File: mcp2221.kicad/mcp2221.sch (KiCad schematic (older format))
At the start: 26 parts, among them J1 Jumper 32 or 21, J2 Conn_01x04_Male, J3 Conn_01x03_Male, J4 Conn_01x06_Male, J5 Conn_01x03_Male, J6 Conn_01x06_Male, J7 Conn_01x02_Male, J8 Conn_01x02_Male, SW1 SW_Push, SW2 SW_Push, U1 AMS1117CD-3.3, U2 MCP2221

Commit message: changed to larger pads on SMD-footprints
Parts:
- C1, C2: footprint Capacitor_SMD:C_1206_3216Metric_Pad1.42x1.75mm_HandSolder -> user:C_1206_3216_Pad1.7x1.75mm_BB
- D1, D2: footprint LED_SMD:LED_1206_3216Metric_Pad1.42x1.75mm_HandSolder -> user:LED_1206_3216_Pad1.7x1.75mm_BB
- R1, R2, R3, R4, R5, R6, R7, R8, R9: footprint Resistor_SMD:R_1206_3216Metric_Pad1.42x1.75mm_HandSolder -> user:R_1206_3216_Pad1.7x1.75mm_BB
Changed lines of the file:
@@
 F 0 "R1" H 4270 3196 50  0000 L CNN
 F 1 "2.2k" H 4270 3105 50  0000 L CNN
-F 2 "Resistor_SMD:R_1206_3216Metric_Pad1.42x1.75mm_HandSolder" V 4130 3150 50  0001 C CNN
+F 2 "user:R_1206_3216_Pad1.7x1.75mm_BB" V 4130 3150 50  0001 C CNN
 F 3 "~" H 4200 3150 50  0001 C CNN
 	1    4200 3150
@@
 F 0 "R2" H 4520 3196 50  0000 L CNN
 F 1 "2.2K" H 4520 3105 50  0000 L CNN
-F 2 "Resistor_SMD:R_1206_3216Metric_Pad1.42x1.75mm_HandSolder" V 4380 3150 50  0001 C CNN
+F 2 "user:R_1206_3216_Pad1.7x1.75mm_BB" V 4380 3150 50  0001 C CNN
 F 3 "~" H 4450 3150 50  0001 C CNN
 	1    4450 3150
@@
 F 0 "R5" H 6450 4100 50  0000 L CNN
 F 1 "1K" H 6450 4000 50  0000 L CNN
-F 2 "Resistor_SMD:R_1206_3216Metric_Pad1.42x1.75mm_HandSolder" V 6580 4050 50  0001 C CNN
+F 2 "user:R_1206_3216_Pad1.7x1.75mm_BB" V 6580 4050 50  0001 C CNN
 F 3 "~" H 6650 4050 50  0001 C CNN
 	1    6650 4050
@@
 F 0 "R6" H 6970 4096 50  0000 L CNN
 F 1 "1K" H 6970 4005 50  0000 L CNN
-F 2 "Resistor_SMD:R_1206_3216Metric_Pad1.42x1.75mm_HandSolder" V 6830 4050 50  0001 C CNN
+F 2 "user:R_1206_3216_Pad1.7x1.75mm_BB" V 6830 4050 50  0001 C CNN
 F 3 "~" H 6900 4050 50  0001 C CNN
 	1    6900 4050
@@
 F 0 "D1" V 6700 4550 50  0000 R CNN
 F 1 "LED" V 6600 4600 50  0000 R CNN
-F 2 "LED_SMD:LED_1206_3216Metric_Pad1.42x1.75mm_HandSolder" H 6650 4350 50  0001 C CNN
+F 2 "user:LED_1206_3216_Pad1.7x1.75mm_BB" H 6650 4350 50  0001 C CNN
 F 3 "~" H 6650 4350 50  0001 C CNN
 	1    6650 4350
@@
 F 0 "D2" V 6939 4233 50  0000 R CNN
 F 1 "LED" V 6848 4233 50  0000 R CNN
-F 2 "LED_SMD:LED_1206_3216Metric_Pad1.42x1.75mm_HandSolder" H 6900 4350 50  0001 C CNN
+F 2 "user:LED_1206_3216_Pad1.7x1.75mm_BB" H 6900 4350 50  0001 C CNN
 F 3 "~" H 6900 4350 50  0001 C CNN
 	1    6900 4350
@@
 F 0 "C2" H 3600 1000 50  0000 C CNN
 F 1 "0.47µF" H 3550 1100 50  0000 C CNN
-F 2 "Capacitor_SMD:C_1206_3216Metric_Pad1.42x1.75mm_HandSolder" H 3888 900 50  0001 C CNN
+F 2 "user:C_1206_3216_Pad1.7x1.75mm_BB" H 3888 900 50  0001 C CNN
 F 3 "~" H 3850 1050 50  0001 C CNN
 	1    3850 1050
@@
 F 0 "R3" H 5570 2596 50  0000 L CNN
 F 1 "10K" H 5570 2505 50  0000 L CNN
-F 2 "Resistor_SMD:R_1206_3216Metric_Pad1.42x1.75mm_HandSolder" V 5430 2550 50  0001 C CNN
+F 2 "user:R_1206_3216_Pad1.7x1.75mm_BB" V 5430 2550 50  0001 C CNN
 F 3 "~" H 5500 2550 50  0001 C CNN
 	1    5500 2550
@@
 F 0 "C1" V 3850 2450 50  0000 C CNN
 F 1 "0.1 µF" V 3950 2450 50  0000 C CNN
-F 2 "Capacitor_SMD:C_1206_3216Metric_Pad1.42x1.75mm_HandSolder" H 3738 2300 50  0001 C CNN
+F 2 "user:C_1206_3216_Pad1.7x1.75mm_BB" H 3738 2300 50  0001 C CNN
 F 3 "~" H 3700 2450 50  0001 C CNN
 	1    3700 2450
@@
 F 0 "R4" H 6570 3496 50  0000 L CNN
 F 1 "4.7K" H 6570 3405 50  0000 L CNN
-F 2 "Resistor_SMD:R_1206_3216Metric_Pad1.42x1.75mm_HandSolder" V 6430 3450 50  0001 C CNN
+F 2 "user:R_1206_3216_Pad1.7x1.75mm_BB" V 6430 3450 50  0001 C CNN
 F 3 "~" H 6500 3450 50  0001 C CNN
 	1    6500 3450
@@
 F 0 "R7" H 7120 3496 50  0000 L CNN
 F 1 "4.7K" H 7120 3405 50  0000 L CNN
-F 2 "Resistor_SMD:R_1206_3216Metric_Pad1.42x1.75mm_HandSolder" V 6980 3450 50  0001 C CNN
+F 2 "user:R_1206_3216_Pad1.7x1.75mm_BB" V 6980 3450 50  0001 C CNN
 F 3 "~" H 7050 3450 50  0001 C CNN
 	1    7050 3450
@@
 F 0 "R8" H 8470 3446 50  0000 L CNN
 F 1 "4.7K" H 8470 3355 50  0000 L CNN
-F 2 "Resistor_SMD:R_1206_3216Metric_Pad1.42x1.75mm_HandSolder" V 8330 3400 50  0001 C CNN
+F 2 "user:R_1206_3216_Pad1.7x1.75mm_BB" V 8330 3400 50  0001 C CNN
 F 3 "~" H 8400 3400 50  0001 C CNN
 	1    8400 3400
@@
 F 0 "R9" H 9020 3446 50  0000 L CNN
 F 1 "4.7K" H 9020 3355 50  0000 L CNN
-F 2 "Resistor_SMD:R_1206_3216Metric_Pad1.42x1.75mm_HandSolder" V 8880 3400 50  0001 C CNN
+F 2 "user:R_1206_3216_Pad1.7x1.75mm_BB" V 8880 3400 50  0001 C CNN
 F 3 "~" H 8950 3400 50  0001 C CNN
 	1    8950 3400

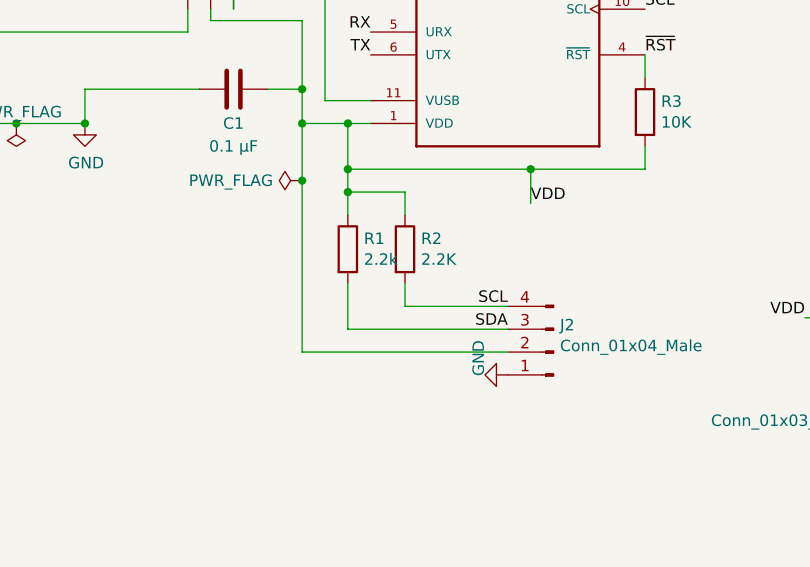
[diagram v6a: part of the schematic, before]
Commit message: changed I2C-connector
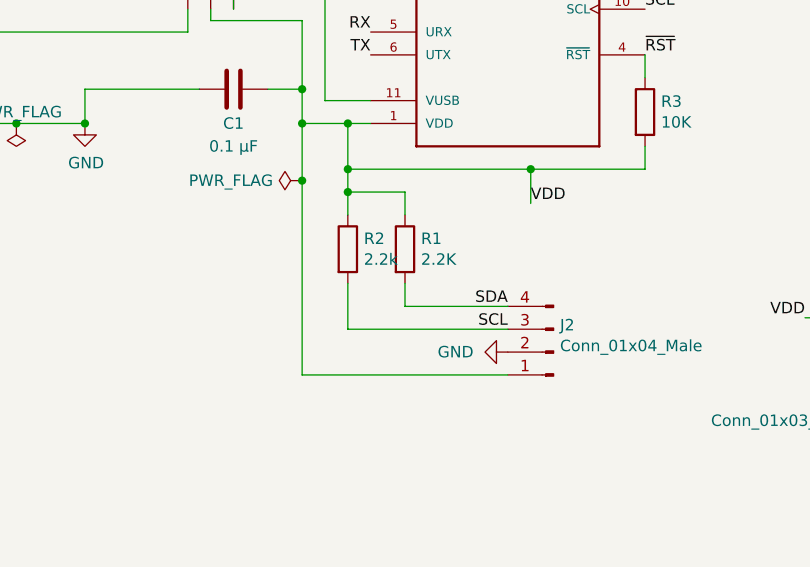
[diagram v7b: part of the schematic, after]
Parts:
- renumbered R2 to R1, R1 to R2
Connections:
- net GND: now also J2.2 (Pin_2); no longer J2.1 (Pin_1)
- net SCL: now also J2.3 (Pin_3), R2.2; no longer J2.4 (Pin_4), R1.2
- net SDA: now also J2.4 (Pin_4), R1.2; no longer J2.3 (Pin_3), R2.2
- net VDD: now also J2.1 (Pin_1); no longer J2.2 (Pin_2)
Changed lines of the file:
@@
 	-1   0    0    1
 $EndComp
+Text Label 4900 3500 2    50   ~ 0
+SCL
 Text Label 4900 3400 2    50   ~ 0
-SCL
-Text Label 4900 3500 2    50   ~ 0
 SDA
 $Comp
 L power:GND #PWR05
 U 1 1 5E4C1242
-P 4900 3700
-F 0 "#PWR05" H 4900 3450 50  0001 C CNN
-F 1 "GND" H 4905 3572 50  0000 R CNN
-F 2 "" H 4900 3700 50  0001 C CNN
-F 3 "" H 4900 3700 50  0001 C CNN
-	1    4900 3700
+P 4900 3600
+F 0 "#PWR05" H 4900 3350 50  0001 C CNN
+F 1 "GND" V 4900 3450 50  0000 R CNN
+F 2 "" H 4900 3600 50  0001 C CNN
+F 3 "" H 4900 3600 50  0001 C CNN
+	1    4900 3600
 	0    1    1    0
 $EndComp
 $Comp
-L Device:R R1
+L Device:R R2
 U 1 1 5E4C2101
 P 4200 3150
-F 0 "R1" H 4270 3196 50  0000 L CNN
+F 0 "R2" H 4270 3196 50  0000 L CNN
 F 1 "2.2k" H 4270 3105 50  0000 L CNN
 F 2 "user:R_1206_3216_Pad1.7x1.75mm_BB" V 4130 3150 50  0001 C CNN
@@
 $EndComp
 $Comp
-L Device:R R2
+L Device:R R1
 U 1 1 5E4C2B00
 P 4450 3150
-F 0 "R2" H 4520 3196 50  0000 L CNN
+F 0 "R1" H 4520 3196 50  0000 L CNN
 F 1 "2.2K" H 4520 3105 50  0000 L CNN
 F 2 "user:R_1206_3216_Pad1.7x1.75mm_BB" V 4380 3150 50  0001 C CNN
@@
 	1    0    0    -1
 $EndComp
-Wire Wire Line
-	4900 3600 4000 3600
 Wire Wire Line
 	4200 3300 4200 3500
@@
 	4000 2600 4000 2850
 Connection ~ 4000 2850
-Wire Wire Line
-	4000 2850 4000 3600
 Wire Wire Line
 	4200 2800 4200 2900
@@
 Wire Wire Line
 	7900 2700 8550 2700
+Wire Wire Line
+	4900 3700 4000 3700
+Wire Wire Line
+	4000 2850 4000 3700
 $EndSCHEMATC
